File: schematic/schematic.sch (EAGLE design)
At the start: 2 parts

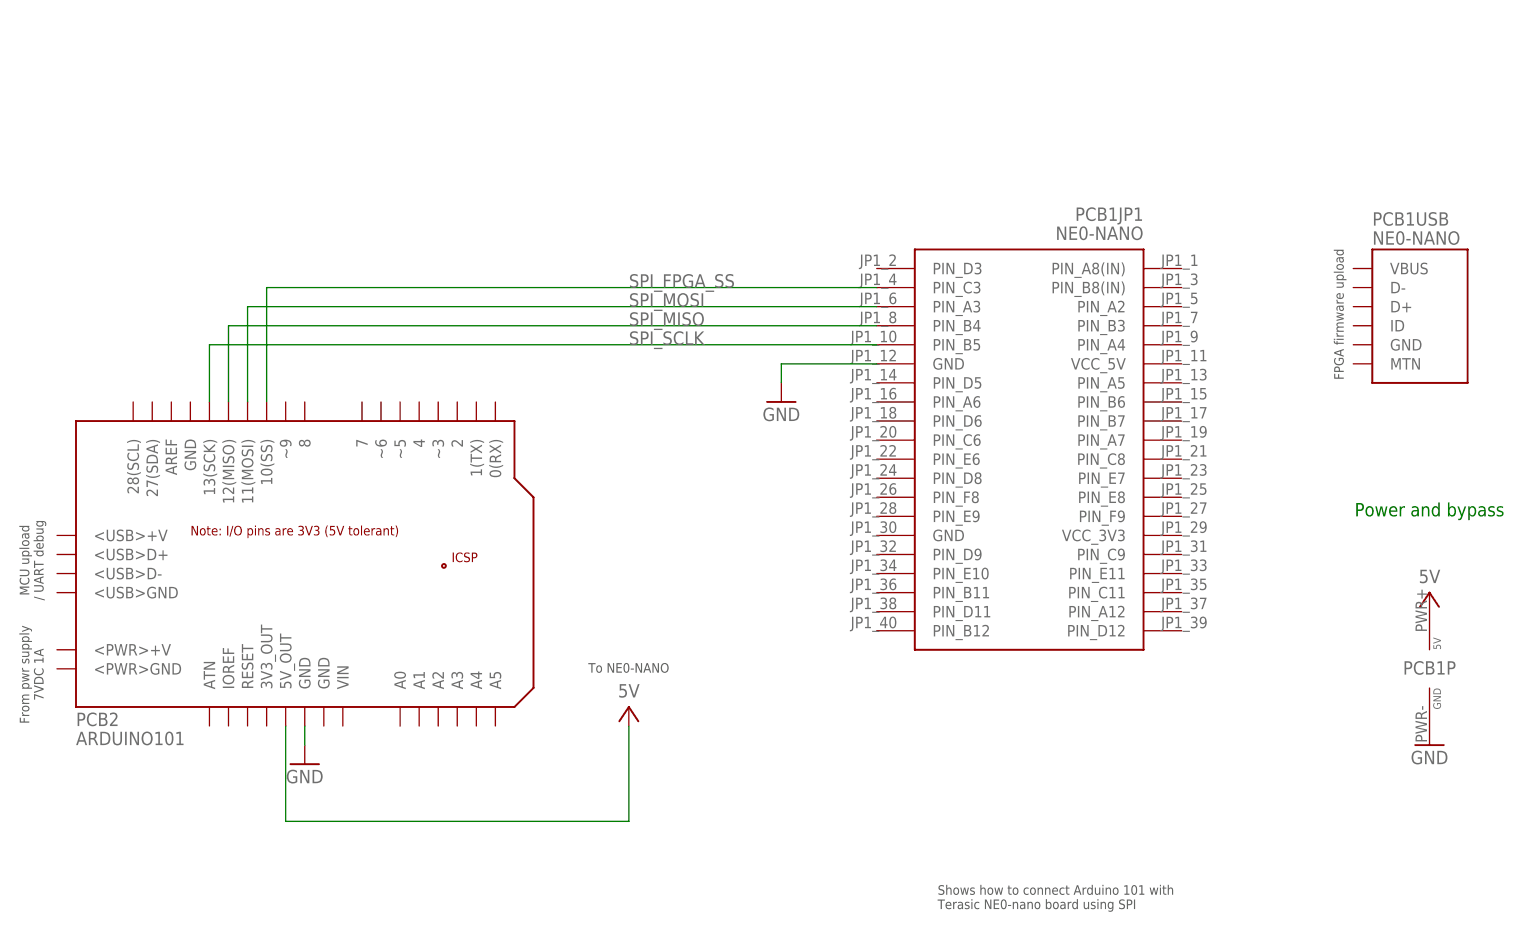
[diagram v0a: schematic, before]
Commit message: update schematic and imgs
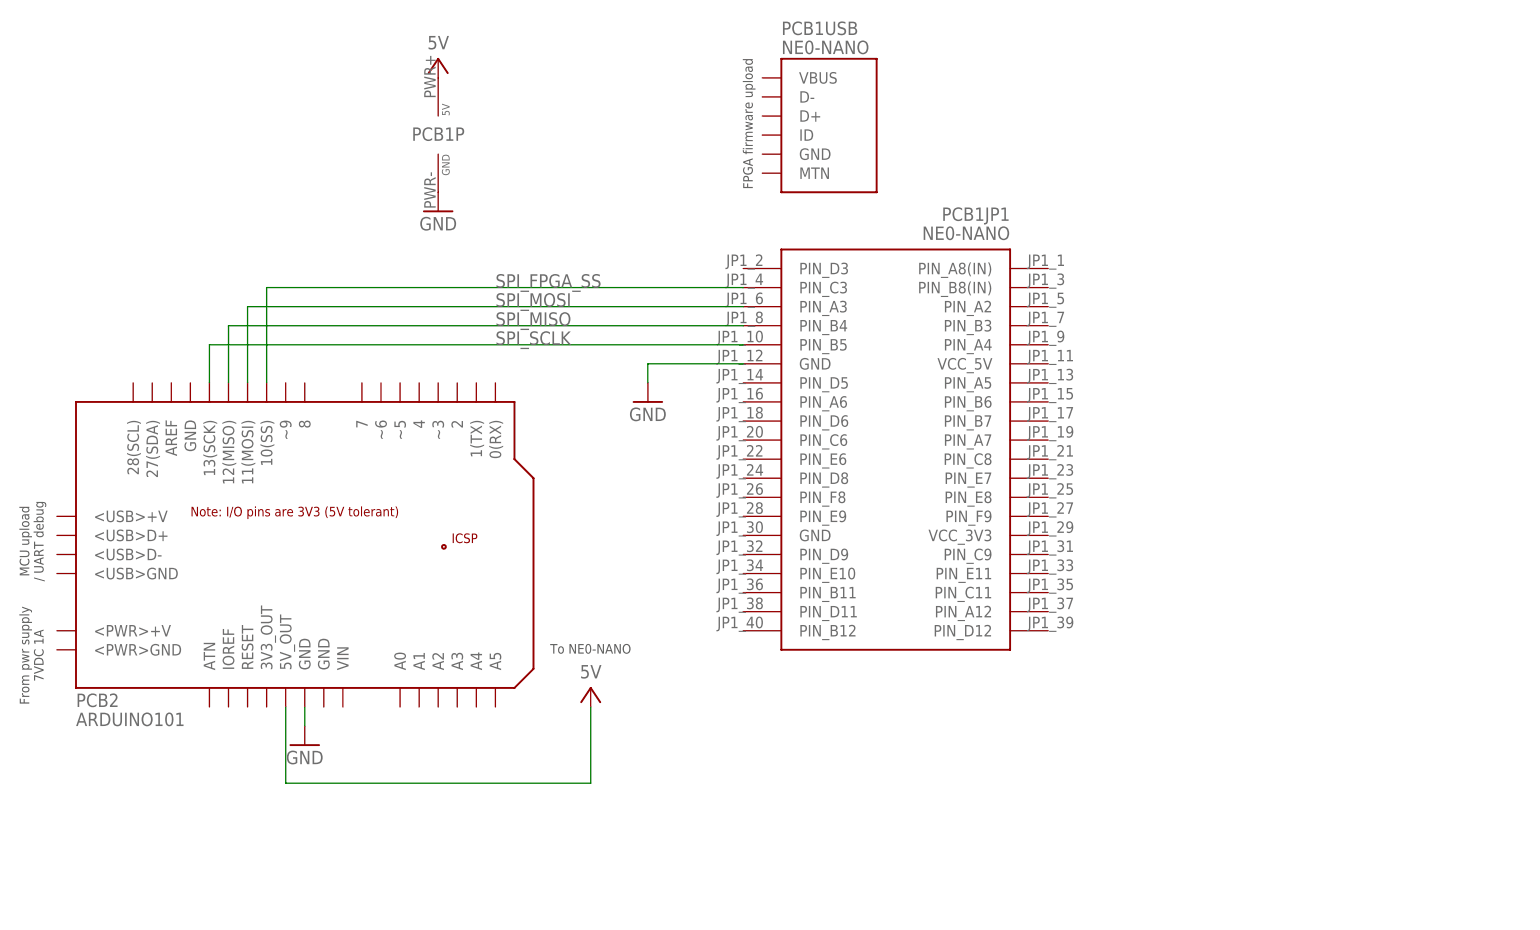
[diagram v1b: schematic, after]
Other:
- note removed: "Power and bypass"
- note removed: "Shows how to connect Arduino 101 with Terasic NE0-nano board using SPI"
- moved on the sheet: PCB1JP1, PCB1P, PCB1USB, PCB2
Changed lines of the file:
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@@
 <?xml version="1.0" encoding="utf-8"?>
 <!DOCTYPE eagle SYSTEM "eagle.dtd">
-<eagle version="7.7.0">
+<eagle version="9.6.2">
 <drawing>
 <settings>
 <setting alwaysvectorfont="no"/>
+<setting keepoldvectorfont="yes"/>
 <setting verticaltext="up"/>
 </settings>
@@
 <part name="GND1" library="Coert Vonk" deviceset="GND" device=""/>
 <part name="GND7" library="Coert Vonk" deviceset="GND" device=""/>
-<part name="U$1" library="Coert Vonk" deviceset="FRAME_LETTER_L" device="">
-<attribute name="AUTHOR_NAME" value="Johan Vonk"/>
-<attribute name="DESCRIPTION" value="Math talk (SPI interface)"/>
-<attribute name="REV" value="0.1"/>
-<attribute name="URL" value="http://www.coertvonk.com"/>
-</part>
 <part name="GND11" library="Coert Vonk" deviceset="GND" device=""/>
 <part name="PCB2" library="Coert Vonk" deviceset="ARDUINO101" device=""/>
@@
 <sheet>
 <plain>
-<text x="36.322" y="37.338" size="1.27" layer="97" rot="R90" align="bottom-center">MCU upload
+<text x="36.322" y="39.878" size="1.27" layer="97" rot="R90" align="bottom-center">MCU upload
 / UART debug</text>
-<text x="209.55" y="70.104" size="1.27" layer="97" rot="R90" align="bottom-center">FPGA firmware upload</text>
-<text x="114.3" y="22.352" size="1.27" layer="97" align="bottom-center">To NE0-NANO</text>
-<text x="220.98" y="43.18" size="1.778" layer="91" align="bottom-center">Power and bypass</text>
-<text x="36.322" y="22.098" size="1.27" layer="97" rot="R90" align="bottom-center">From pwr supply
+<text x="130.81" y="95.504" size="1.27" layer="97" rot="R90" align="bottom-center">FPGA firmware upload</text>
+<text x="109.22" y="24.892" size="1.27" layer="97" align="bottom-center">To NE0-NANO</text>
+<text x="36.322" y="24.638" size="1.27" layer="97" rot="R90" align="bottom-center">From pwr supply
 7VDC 1A</text>
-<text x="155.448" y="-9.144" size="1.27" layer="97">Shows how to connect Arduino 101 with
-Terasic NE0-nano board using SPI</text>
 </plain>
 <instances>
-<instance part="P+6" gate="1" x="220.98" y="33.02"/>
-<instance part="P+7" gate="1" x="114.3" y="17.78"/>
-<instance part="GND1" gate="1" x="71.12" y="10.16"/>
-<instance part="GND7" gate="1" x="220.98" y="12.7"/>
-<instance part="U$1" gate="G$1" x="0" y="-20.32"/>
-<instance part="U$1" gate="G$2" x="147.32" y="-20.32">
-<attribute name="URL" x="147.32" y="-20.32" size="1.778" layer="96" display="off"/>
-<attribute name="REV" x="147.32" y="-20.32" size="1.778" layer="96" display="off"/>
-</instance>
-<instance part="GND11" gate="1" x="134.62" y="58.42"/>
-<instance part="PCB2" gate="G$1" x="40.64" y="17.78"/>
-<instance part="PCB1" gate="JP1" x="182.88" y="25.4" rot="MR0"/>
-<instance part="PCB1" gate="P" x="220.98" y="22.86"/>
-<instance part="PCB1" gate="USB" x="213.36" y="66.04"/>
+<instance part="P+6" gate="1" x="88.9" y="104.14" smashed="yes">
+<attribute name="VALUE" x="88.9" y="105.41" size="1.778" layer="96" align="bottom-center"/>
+</instance>
+<instance part="P+7" gate="1" x="109.22" y="20.32" smashed="yes">
+<attribute name="VALUE" x="109.22" y="21.59" size="1.778" layer="96" align="bottom-center"/>
+</instance>
+<instance part="GND1" gate="1" x="71.12" y="12.7" smashed="yes">
+<attribute name="VALUE" x="71.12" y="10.16" size="1.778" layer="96" align="bottom-center"/>
+</instance>
+<instance part="GND7" gate="1" x="88.9" y="83.82" smashed="yes">
+<attribute name="VALUE" x="88.9" y="81.28" size="1.778" layer="96" align="bottom-center"/>
+</instance>
+<instance part="GND11" gate="1" x="116.84" y="58.42" smashed="yes">
+<attribute name="VALUE" x="116.84" y="55.88" size="1.778" layer="96" align="bottom-center"/>
+</instance>
+<instance part="PCB2" gate="G$1" x="40.64" y="20.32" smashed="yes">
+<attribute name="NAME" x="40.64" y="17.78" size="1.778" layer="95"/>
+<attribute name="VALUE" x="40.64" y="15.24" size="1.778" layer="96"/>
+</instance>
+<instance part="PCB1" gate="JP1" x="165.1" y="25.4" smashed="yes" rot="MR0">
+<attribute name="NAME" x="165.1" y="82.55" size="1.778" layer="95" rot="MR0"/>
+<attribute name="VALUE" x="165.1" y="80.01" size="1.778" layer="96" rot="MR0"/>
+</instance>
+<instance part="PCB1" gate="P" x="88.9" y="93.98" smashed="yes">
+<attribute name="NAME" x="88.9" y="93.218" size="1.778" layer="95" align="bottom-center"/>
+</instance>
+<instance part="PCB1" gate="USB" x="134.62" y="91.44" smashed="yes">
+<attribute name="NAME" x="134.62" y="107.315" size="1.778" layer="95"/>
+<attribute name="VALUE" x="134.62" y="104.775" size="1.778" layer="96"/>
+</instance>
 </instances>
 <busses>
@@
 <net name="+5V" class="0">
 <segment>
-<wire x1="68.58" y1="2.54" x2="68.58" y2="15.24" width="0.1524" layer="91"/>
+<wire x1="68.58" y1="7.62" x2="68.58" y2="17.78" width="0.1524" layer="91"/>
 <pinref part="P+7" gate="1" pin="+5V"/>
-<wire x1="68.58" y1="2.54" x2="114.3" y2="2.54" width="0.1524" layer="91"/>
-<wire x1="114.3" y1="2.54" x2="114.3" y2="15.24" width="0.1524" layer="91"/>
+<wire x1="68.58" y1="7.62" x2="109.22" y2="7.62" width="0.1524" layer="91"/>
+<wire x1="109.22" y1="7.62" x2="109.22" y2="17.78" width="0.1524" layer="91"/>
 <pinref part="PCB2" gate="G$1" pin="5V_OUT"/>
 </segment>
@@
 <segment>
 <pinref part="GND1" gate="1" pin="GND"/>
-<wire x1="71.12" y1="15.24" x2="71.12" y2="12.7" width="0.1524" layer="91"/>
+<wire x1="71.12" y1="17.78" x2="71.12" y2="15.24" width="0.1524" layer="91"/>
 <pinref part="PCB2" gate="G$1" pin="GND@1"/>
 </segment>
 <segment>
 <pinref part="GND11" gate="1" pin="GND"/>
-<wire x1="147.32" y1="63.5" x2="134.62" y2="63.5" width="0.1524" layer="91"/>
-<wire x1="134.62" y1="63.5" x2="134.62" y2="60.96" width="0.1524" layer="91"/>
+<wire x1="129.54" y1="63.5" x2="116.84" y2="63.5" width="0.1524" layer="91"/>
+<wire x1="116.84" y1="63.5" x2="116.84" y2="60.96" width="0.1524" layer="91"/>
 <pinref part="PCB1" gate="JP1" pin="GND@1"/>
 </segment>
@@
 <net name="SPI_SCLK" class="0">
 <segment>
-<wire x1="58.42" y1="58.42" x2="58.42" y2="66.04" width="0.1524" layer="91"/>
-<wire x1="58.42" y1="66.04" x2="147.32" y2="66.04" width="0.1524" layer="91"/>
-<label x="114.3" y="66.04" size="1.778" layer="95"/>
+<wire x1="58.42" y1="60.96" x2="58.42" y2="66.04" width="0.1524" layer="91"/>
+<wire x1="58.42" y1="66.04" x2="129.54" y2="66.04" width="0.1524" layer="91"/>
+<label x="96.52" y="66.04" size="1.778" layer="95"/>
 <pinref part="PCB2" gate="G$1" pin="13(SCK)"/>
 <pinref part="PCB1" gate="JP1" pin="PIN_B5"/>
@@
 <net name="SPI_MISO" class="0">
 <segment>
-<wire x1="60.96" y1="58.42" x2="60.96" y2="68.58" width="0.1524" layer="91"/>
-<wire x1="60.96" y1="68.58" x2="147.32" y2="68.58" width="0.1524" layer="91"/>
-<label x="114.3" y="68.58" size="1.778" layer="95"/>
+<wire x1="60.96" y1="60.96" x2="60.96" y2="68.58" width="0.1524" layer="91"/>
+<wire x1="60.96" y1="68.58" x2="129.54" y2="68.58" width="0.1524" layer="91"/>
+<label x="96.52" y="68.58" size="1.778" layer="95"/>
 <pinref part="PCB2" gate="G$1" pin="12(MISO)"/>
 <pinref part="PCB1" gate="JP1" pin="PIN_B4"/>
@@
 <net name="SPI_MOSI" class="0">
 <segment>
-<wire x1="63.5" y1="58.42" x2="63.5" y2="71.12" width="0.1524" layer="91"/>
-<wire x1="63.5" y1="71.12" x2="147.32" y2="71.12" width="0.1524" layer="91"/>
-<label x="114.3" y="71.12" size="1.778" layer="95"/>
+<wire x1="63.5" y1="60.96" x2="63.5" y2="71.12" width="0.1524" layer="91"/>
+<wire x1="63.5" y1="71.12" x2="129.54" y2="71.12" width="0.1524" layer="91"/>
+<label x="96.52" y="71.12" size="1.778" layer="95"/>
 <pinref part="PCB2" gate="G$1" pin="11(MOSI)"/>
 <pinref part="PCB1" gate="JP1" pin="PIN_A3"/>
@@
 <net name="SPI_FPGA_SS" class="0">
 <segment>
-<wire x1="66.04" y1="58.42" x2="66.04" y2="73.66" width="0.1524" layer="91"/>
-<wire x1="66.04" y1="73.66" x2="147.32" y2="73.66" width="0.1524" layer="91"/>
-<label x="114.3" y="73.66" size="1.778" layer="95"/>
+<wire x1="66.04" y1="60.96" x2="66.04" y2="73.66" width="0.1524" layer="91"/>
+<wire x1="66.04" y1="73.66" x2="129.54" y2="73.66" width="0.1524" layer="91"/>
+<label x="96.52" y="73.66" size="1.778" layer="95"/>
 <pinref part="PCB2" gate="G$1" pin="10(SS)"/>
 <pinref part="PCB1" gate="JP1" pin="PIN_C3"/>
